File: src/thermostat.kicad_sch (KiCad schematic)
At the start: 113 parts, among them U18 AD5680, U19 MAX1968xUI, U20 RS8552, U21 TLV9001IDCK, U22 AD7172-2, U23 AD7172-4BCPZ

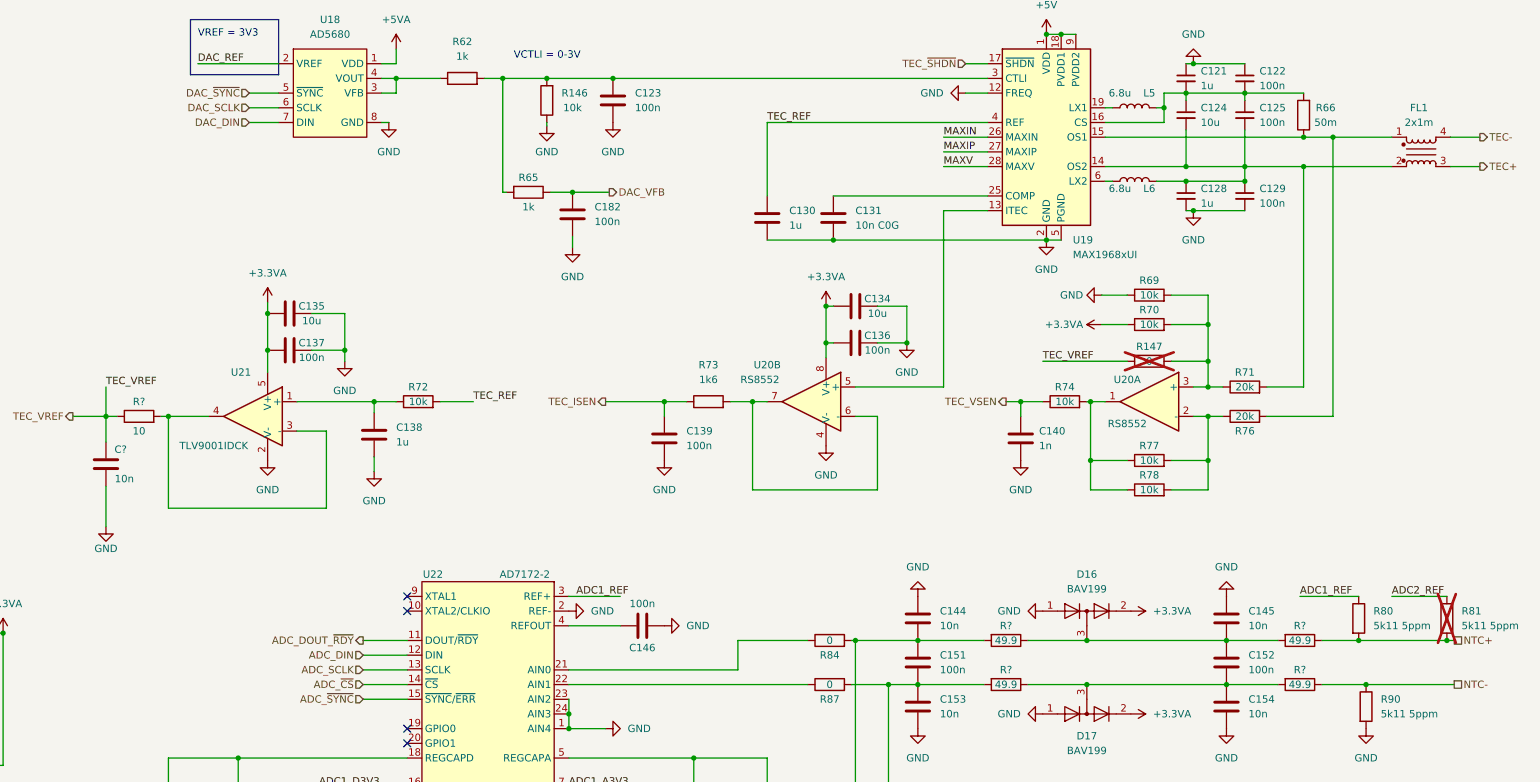
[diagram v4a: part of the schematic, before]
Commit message: Fix issiues from lis, see bug/issiue list in DOC directory
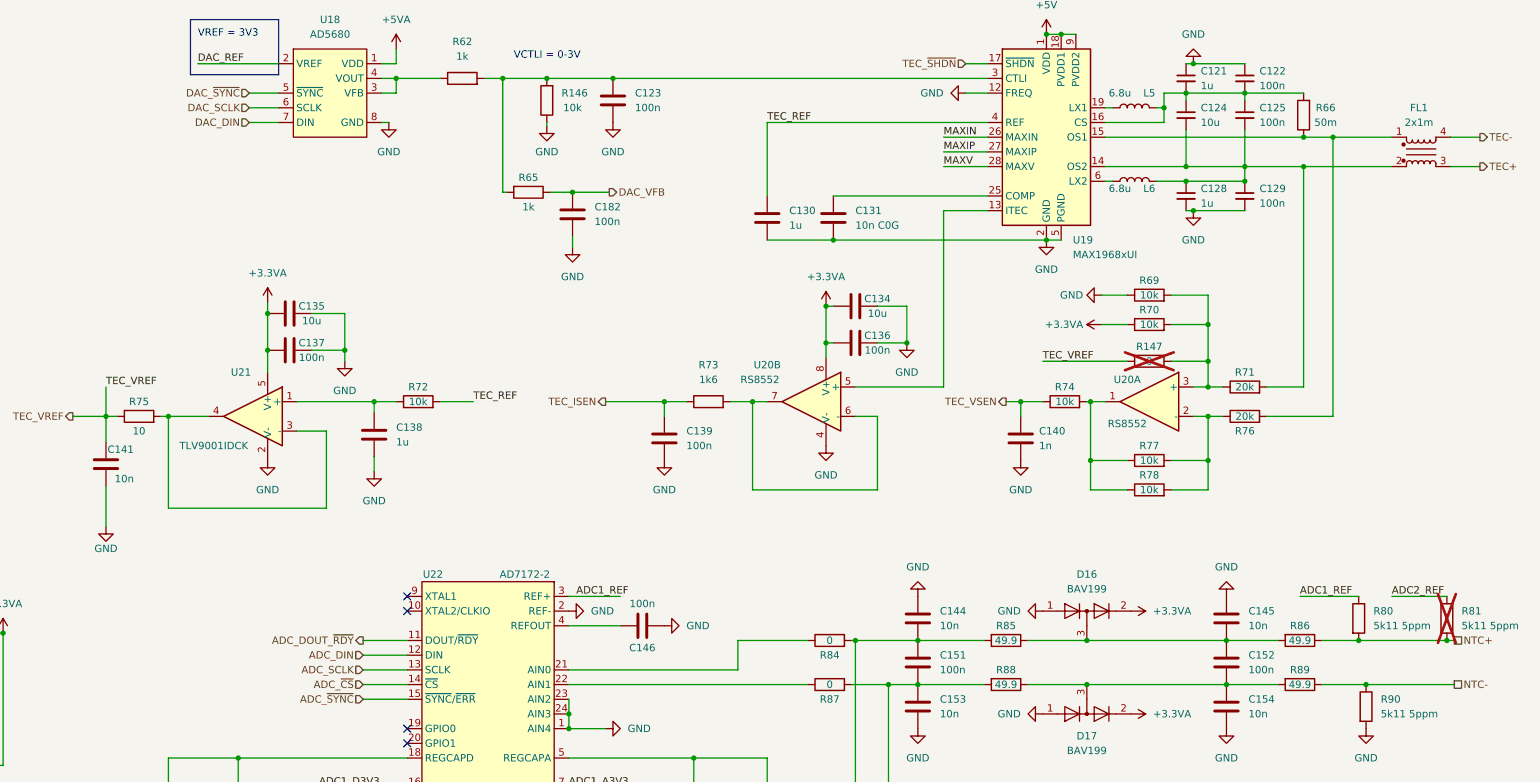
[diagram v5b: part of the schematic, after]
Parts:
- gave numbers to parts that had none: 6
